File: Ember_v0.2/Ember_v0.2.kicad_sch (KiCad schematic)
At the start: 87 parts, among them J3 DROGUE, J4 BATT_CONN, J5 MAIN, J6 MAN2, J7 DROGUE2, J8 ARM, Q1 SISA96DN-T1, Q2 SISA96DN-T1, Q3 SISA96DN-T1, Q4 SISA96DN-T1, Q5 CJ3400, U1 LDO Regulator 5v, U2 BNO055, U4 BMP280, U6 ADS1220xPW, U7 RPi Pico 2, U8 ADS1220xPW

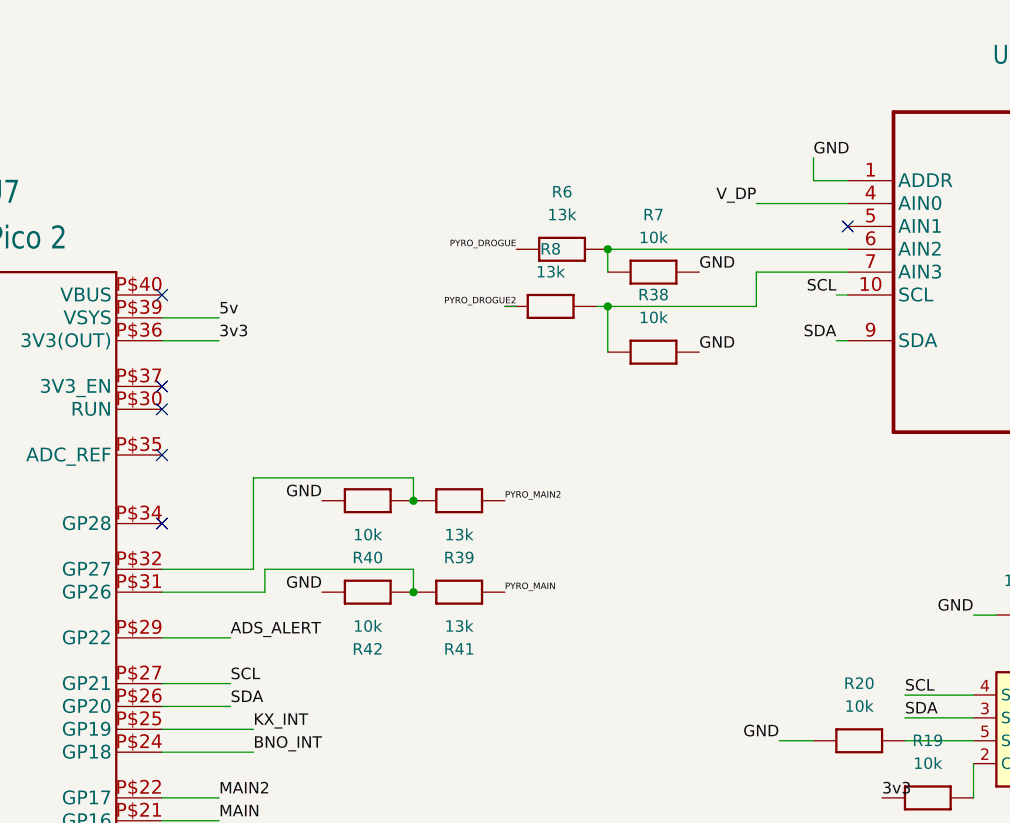
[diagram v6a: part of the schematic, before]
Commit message: Some changes on V0.2 layout
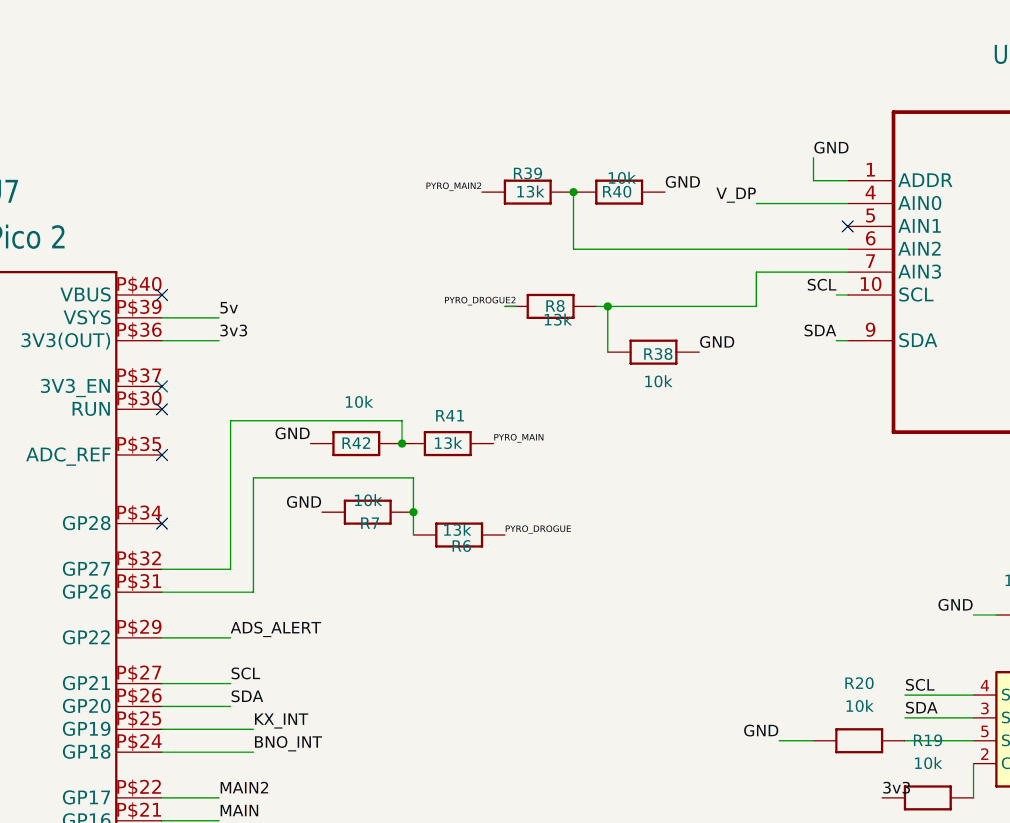
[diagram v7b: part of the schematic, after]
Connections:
- net at R39.2, R40.1: now also U5.6 (AIN2); no longer U7.P$32 (GP27)
- net at R41.2, R42.1: now also U7.P$32 (GP27); no longer U7.P$31 (GP26)
- net at R6.2, R7.1: now also U7.P$31 (GP26); no longer U5.6 (AIN2)
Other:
- moved on the sheet: R39, R40, R41, R42, R6, R7

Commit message: board route almost complete
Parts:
- added 11111111111111111, 12111111111111111: ~, microbuilder:MOUNTINGHOLE_3.0_PLATED, symbol microbuilder:MOUNTINGHOLE
- added JP6: ~, microbuilder:1X02_OVAL, symbol microbuilder:HEADER-1X2
- added Q6: SISA96DN-T1, SISA96DN-T1-GE3:SIS862DNT1GE3, symbol SISA96DN-T1-GE3:SISA96DN-T1-GE3
- added R23: 33k, microbuilder:0603, symbol microbuilder:RESISTOR0603
- added R24: 1k, microbuilder:0603, symbol microbuilder:RESISTOR0603
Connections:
- net GND: now also Q6.1 (S_1), Q6.2 (S_2), Q6.3 (S_3), R23.2
- net V_BATT: now also JP6.2
- net CAM: now reaches U7.P$5 (GP3)
- net CAM: now also R24.1
- new net: Q6.4 (G), R23.1, R24.2
- new net CAM_OUT: JP6.1, Q6.10 (D_6), Q6.11 (D_7), Q6.5 (D_1), Q6.6 (D_2), Q6.7 (D_3), Q6.8 (D_4), Q6.9 (D_5)
- no-connect marks 18 -> 17
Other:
- moved on the sheet: Q1, Q2, Q3, Q4, R28, R29, R30, R31, R32, R33, R4, R5
